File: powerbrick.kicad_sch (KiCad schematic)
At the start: 4 parts, among them U4 TLV62568DBV

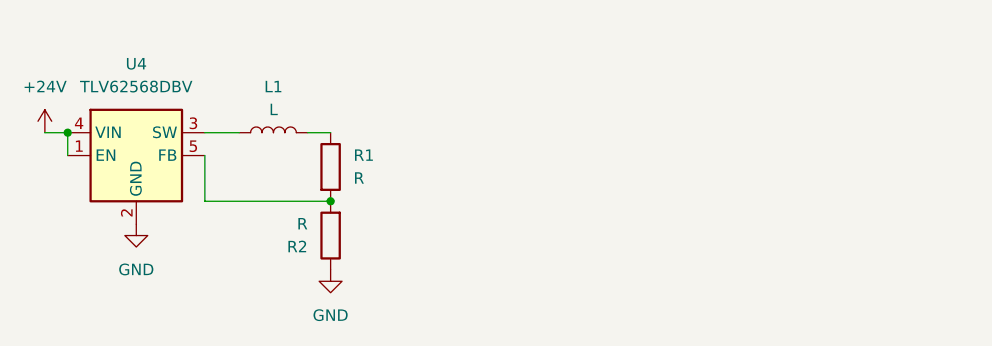
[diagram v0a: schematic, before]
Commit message: power to ICs
updated power brick. added CMOS battery
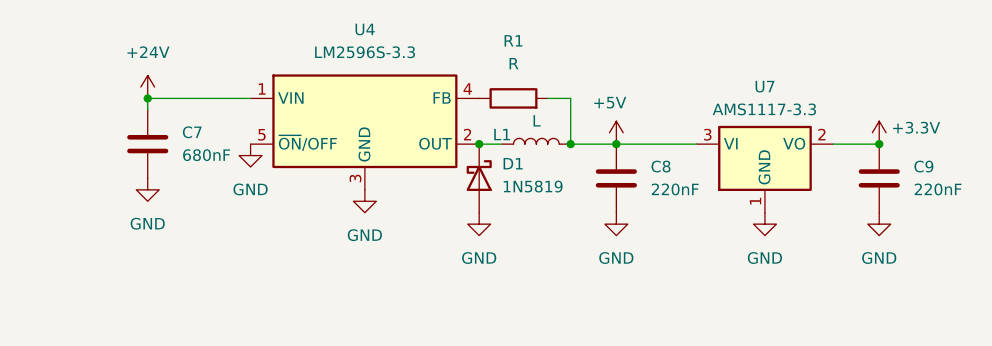
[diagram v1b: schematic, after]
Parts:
- removed R2: R, symbol Device:R
- removed U4: TLV62568DBV, Package_TO_SOT_SMD:SOT-23-5, symbol Regulator_Switching:TLV62568DBV
- added C7: 680nF, symbol Device:C
- added C8, C9: 220nF, symbol Device:C
- added D1: 1N5819, Diode_THT:D_DO-41_SOD81_P10.16mm_Horizontal, symbol Diode:1N5819
- added U4: LM2596S-3.3, Package_TO_SOT_SMD:TO-263-5_TabPin3, symbol Regulator_Switching:LM2596S-3.3
- added U7: AMS1117-3.3, Package_TO_SOT_SMD:SOT-223-3_TabPin2, symbol Regulator_Linear:AMS1117-3.3
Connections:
- net +24V: now also C7.1, U4.1 (VIN)
- net GND: now also C7.2, C8.2, C9.2, D1.2 (A), U4.3 (GND), U4.5 (~{ON}/OFF), U7.1 (GND)
- net at R1.1: now also U4.4 (FB); no longer L1.2
- net +5V: now reaches R1.2
- net +5V: now also L1.2, C8.1, U7.3 (VI)
- net at L1.1: now also D1.1 (K), U4.2 (OUT)
- new net +3.3V: C9.1, U7.2 (VO)
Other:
- moved on the sheet: L1

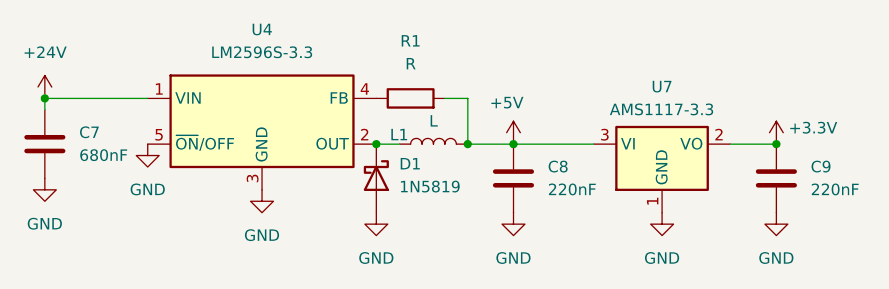
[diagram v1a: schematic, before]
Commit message: Values and finishing touches
I ve seen you put bad values for capacitors in powerbrick and added the value of the feedback resistor, also I redid the inductor circuit because gemini said so and your mosfet was for 20 V not 24 V ...
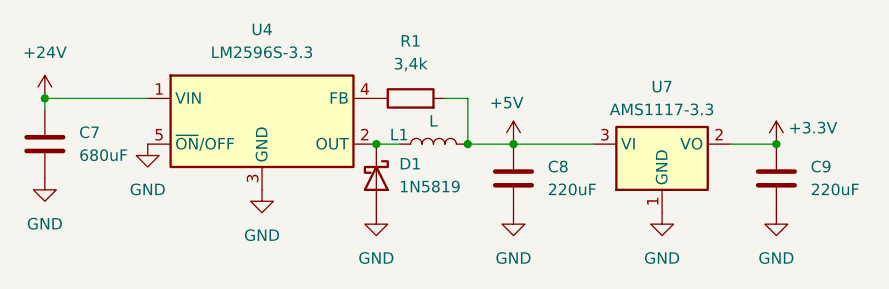
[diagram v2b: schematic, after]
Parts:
- C7: value 680nF -> 680uF
- C8, C9: value 220nF -> 220uF
- R1: value R -> 3,4k
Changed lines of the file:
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@@
 			)
 		)
-		(property "Value" "R"
+		(property "Value" "3,4k"
 			(at 111.76 31.75 90)
 			(effects
@@
 			)
 		)
-		(property "Value" "680nF"
+		(property "Value" "680uF"
 			(at 74.93 41.9099 0)
 			(effects
@@
 			)
 		)
-		(property "Value" "220nF"
+		(property "Value" "220uF"
 			(at 156.21 45.7199 0)
 			(effects
@@
 			)
 		)
-		(property "Value" "220nF"
+		(property "Value" "220uF"
 			(at 127 45.7199 0)
 			(effects

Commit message: .
označení sekcí
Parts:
- added C10: 220nF, symbol Device:C
- C9: value 220uF -> 220nF
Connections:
- net +5V: now also C10.1
- net GND: now also C10.2
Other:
- moved on the sheet: C9, U7
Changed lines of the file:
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@@
 	)
 	(junction
-		(at 152.4 40.64)
+		(at 165.1 40.64)
+		(diameter 0)
+		(color 0 0 0 0)
+	)
+	(junction
+		(at 135.89 40.64)
 		(diameter 0)
 		(color 0 0 0 0)
@@
 	(wire
 		(pts
-			(xy 123.19 40.64) (xy 132.08 40.64)
+			(xy 123.19 40.64) (xy 135.89 40.64)
 		)
 		(stroke
@@
 	(wire
 		(pts
-			(xy 71.12 35.56) (xy 71.12 36.83)
+			(xy 135.89 40.64) (xy 144.78 40.64)
 		)
 		(stroke
@@
 	(wire
 		(pts
-			(xy 118.11 35.56) (xy 118.11 40.64)
+			(xy 71.12 35.56) (xy 71.12 36.83)
 		)
 		(stroke
@@
 	(wire
 		(pts
-			(xy 71.12 35.56) (xy 82.55 35.56)
+			(xy 118.11 35.56) (xy 118.11 40.64)
 		)
 		(stroke
@@
 	(wire
 		(pts
-			(xy 118.11 40.64) (xy 123.19 40.64)
+			(xy 71.12 35.56) (xy 82.55 35.56)
 		)
 		(stroke
@@
 	(wire
 		(pts
-			(xy 152.4 40.64) (xy 147.32 40.64)
+			(xy 118.11 40.64) (xy 123.19 40.64)
 		)
 		(stroke
@@
 		)
 	)
+	(wire
+		(pts
+			(xy 165.1 40.64) (xy 160.02 40.64)
+		)
+		(stroke
+			(width 0)
+			(type default)
+		)
+	)
 	(symbol
 		(lib_id "Device:R")
@@
 	)
 	(symbol
+		(lib_id "Device:C")
+		(at 135.89 44.45 0)
+		(unit 1)
+		(exclude_from_sim no)
+		(in_bom yes)
+		(on_board yes)
+		(dnp no)
+		(fields_autoplaced yes)
+		(property "Reference" "C10"
+			(at 139.7 43.1799 0)
+			(effects
+				(font
+					(size 1.27 1.27)
+				)
+				(justify left)
+			)
+		)
+		(property "Value" "220nF"
+			(at 139.7 45.7199 0)
+			(effects
+				(font
+					(size 1.27 1.27)
+				)
+				(justify left)
+			)
+		)
+		(property "Footprint" ""
+			(at 136.8552 48.26 0)
+			(effects
+				(font
+					(size 1.27 1.27)
+				)
+				(hide yes)
+			)
+		)
+		(property "Datasheet" "~"
+			(at 135.89 44.45 0)
+			(effects
+				(font
+					(size 1.27 1.27)
+				)
+				(hide yes)
+			)
+		)
+		(property "Description" "Unpolarized capacitor"
+			(at 135.89 44.45 0)
+			(effects
+				(font
+					(size 1.27 1.27)
+				)
+				(hide yes)
+			)
+		)
+		(pin "1"
+		)
+		(pin "2"
+		)
+		(instances
+			(project "TechStarter"
+				(path "/7ea2363f-6757-4fc6-83f2-16ce190d79d1/efa4ad20-026b-4f4f-bd8d-a347b34e01c5"
+					(reference "C10")
+					(unit 1)
+				)
+			)
+		)
+	)
+	(symbol
 		(lib_id "power:GND")
 		(at 123.19 48.26 0)
@@
 	(symbol
 		(lib_id "power:+3.3V")
-		(at 152.4 40.64 0)
+		(at 165.1 40.64 0)
 		(unit 1)
 		(exclude_from_sim no)
@@
 		(dnp no)
 		(property "Reference" "#PWR032"
-			(at 152.4 44.45 0)
+			(at 165.1 44.45 0)
 			(effects
 				(font
@@
 		)
 		(property "Value" "+3.3V"
-			(at 156.464 38.862 0)
-			(effects
-				(font
-					(size 1.27 1.27)
-				)
-			)
-		)
-		(property "Footprint" ""
-			(at 152.4 40.64 0)
+			(at 169.164 38.862 0)
+			(effects
+				(font
+					(size 1.27 1.27)
+				)
+			)
+		)
+		(property "Footprint" ""
+			(at 165.1 40.64 0)
 			(effects
 				(font
@@
 		)
 		(property "Datasheet" ""
-			(at 152.4 40.64 0)
+			(at 165.1 40.64 0)
 			(effects
 				(font
@@
 		)
 		(property "Description" "Power symbol creates a global label with name \"+3.3V\""
-			(at 152.4 40.64 0)
+			(at 165.1 40.64 0)
 			(effects
 				(font
@@
 	(symbol
 		(lib_id "power:GND")
-		(at 139.7 48.26 0)
+		(at 152.4 48.26 0)
 		(unit 1)
 		(exclude_from_sim no)
@@
 		(fields_autoplaced yes)
 		(property "Reference" "#PWR027"
-			(at 139.7 54.61 0)
+			(at 152.4 54.61 0)
 			(effects
 				(font
@@
 		)
 		(property "Value" "GND"
-			(at 139.7 53.34 0)
-			(effects
-				(font
-					(size 1.27 1.27)
-				)
-			)
-		)
-		(property "Footprint" ""
-			(at 139.7 48.26 0)
+			(at 152.4 53.34 0)
+			(effects
+				(font
+					(size 1.27 1.27)
+				)
+			)
+		)
+		(property "Footprint" ""
+			(at 152.4 48.26 0)
 			(effects
 				(font
@@
 		)
 		(property "Datasheet" ""
-			(at 139.7 48.26 0)
+			(at 152.4 48.26 0)
 			(effects
 				(font
@@
 		)
 		(property "Description" "Power symbol creates a global label with name \"GND\" , ground"
-			(at 139.7 48.26 0)
+			(at 152.4 48.26 0)
 			(effects
 				(font
@@
 	(symbol
 		(lib_id "power:GND")
-		(at 152.4 48.26 0)
+		(at 165.1 48.26 0)
 		(unit 1)
 		(exclude_from_sim no)
@@
 		(fields_autoplaced yes)
 		(property "Reference" "#PWR030"
-			(at 152.4 54.61 0)
+			(at 165.1 54.61 0)
 			(effects
 				(font
@@
 		)
 		(property "Value" "GND"
-			(at 152.4 53.34 0)
-			(effects
-				(font
-					(size 1.27 1.27)
-				)
-			)
-		)
-		(property "Footprint" ""
-			(at 152.4 48.26 0)
+			(at 165.1 53.34 0)
+			(effects
+				(font
+					(size 1.27 1.27)
+				)
+			)
+		)
+		(property "Footprint" ""
+			(at 165.1 48.26 0)
 			(effects
 				(font
@@
 		)
 		(property "Datasheet" ""
-			(at 152.4 48.26 0)
+			(at 165.1 48.26 0)
 			(effects
 				(font
@@
 		)
 		(property "Description" "Power symbol creates a global label with name \"GND\" , ground"
-			(at 152.4 48.26 0)
+			(at 165.1 48.26 0)
 			(effects
 				(font
@@
 	)
 	(symbol
+		(lib_id "power:GND")
+		(at 135.89 48.26 0)
+		(unit 1)
+		(exclude_from_sim no)
+		(in_bom yes)
+		(on_board yes)
+		(dnp no)
+		(fields_autoplaced yes)
+		(property "Reference" "#PWR057"
+			(at 135.89 54.61 0)
+			(effects
+				(font
+					(size 1.27 1.27)
+				)
+				(hide yes)
+			)
+		)
+		(property "Value" "GND"
+			(at 135.89 53.34 0)
+			(effects
+				(font
+					(size 1.27 1.27)
+				)
+			)
+		)
+		(property "Footprint" ""
+			(at 135.89 48.26 0)
+			(effects
+				(font
+					(size 1.27 1.27)
+				)
+				(hide yes)
+			)
+		)
+		(property "Datasheet" ""
+			(at 135.89 48.26 0)
+			(effects
+				(font
+					(size 1.27 1.27)
+				)
+				(hide yes)
+			)
+		)
+		(property "Description" "Power symbol creates a global label with name \"GND\" , ground"
+			(at 135.89 48.26 0)
+			(effects
+				(font
+					(size 1.27 1.27)
+				)
+				(hide yes)
+			)
+		)
+		(pin "1"
+		)
+		(instances
+			(project "TechStarter"
+				(path "/7ea2363f-6757-4fc6-83f2-16ce190d79d1/efa4ad20-026b-4f4f-bd8d-a347b34e01c5"
+					(reference "#PWR057")
+					(unit 1)
+				)
+			)
+		)
+	)
+	(symbol
 		(lib_id "Device:C")
-		(at 152.4 44.45 0)
+		(at 165.1 44.45 0)
 		(unit 1)
 		(exclude_from_sim no)
@@
 		(fields_autoplaced yes)
 		(property "Reference" "C9"
-			(at 156.21 43.1799 0)
+			(at 168.91 43.1799 0)
 			(effects
 				(font
@@
 			)
 		)
-		(property "Value" "220uF"
-			(at 156.21 45.7199 0)
+		(property "Value" "220nF"
+			(at 168.91 45.7199 0)
 			(effects
 				(font
@@
 		)
 		(property "Footprint" ""
-			(at 153.3652 48.26 0)
+			(at 166.0652 48.26 0)
 			(effects
 				(font
@@
 		)
 		(property "Datasheet" "~"
-			(at 152.4 44.45 0)
+			(at 165.1 44.45 0)
 			(effects
 				(font
@@
 		)
 		(property "Description" "Unpolarized capacitor"
-			(at 152.4 44.45 0)
+			(at 165.1 44.45 0)
 			(effects
 				(font
@@
 	(symbol
 		(lib_id "Regulator_Linear:AMS1117-3.3")
-		(at 139.7 40.64 0)
+		(at 152.4 40.64 0)
 		(unit 1)
 		(exclude_from_sim no)
@@
 		(fields_autoplaced yes)
 		(property "Reference" "U7"
-			(at 139.7 34.29 0)
+			(at 152.4 34.29 0)
 			(effects
 				(font
@@
 		)
 		(property "Value" "AMS1117-3.3"
-			(at 139.7 36.83 0)
+			(at 152.4 36.83 0)
 			(effects
 				(font
@@
 		)
 		(property "Footprint" "Package_TO_SOT_SMD:SOT-223-3_TabPin2"
-			(at 139.7 35.56 0)
+			(at 152.4 35.56 0)
 			(effects
 				(font
@@
 		)
 		(property "Datasheet" "http://www.advanced-monolithic.com/pdf/ds1117.pdf"
-			(at 142.24 46.99 0)
+			(at 154.94 46.99 0)
 			(effects
 				(font
@@
 		)
 		(property "Description" "1A Low Dropout regulator, positive, 3.3V fixed output, SOT-223"
-			(at 139.7 40.64 0)
-			(effects
-				(font
+			(at 152.4 40.64 0)
+			(effects
+				(font

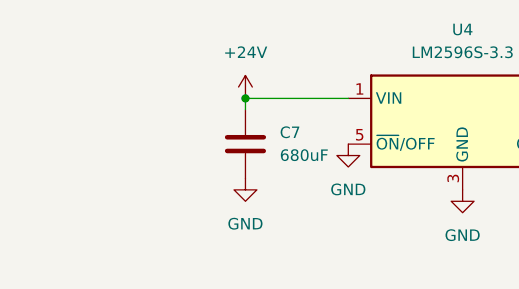
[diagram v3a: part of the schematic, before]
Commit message: Robot I/O
připojil jsem výstup a input z robota přes optočleny a přidal konektor na napájení 24 V
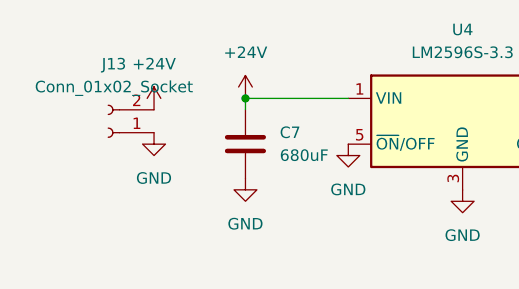
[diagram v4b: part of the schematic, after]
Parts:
- added J13: Conn_01x02_Socket, symbol Connector:Conn_01x02_Socket
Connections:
- net +24V: now also J13.2 (Pin_2)
- net GND: now also J13.1 (Pin_1)
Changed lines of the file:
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@@
+	)
+	(symbol
+		(lib_id "power:+24V")
+		(at 60.96 36.83 0)
+		(unit 1)
+		(exclude_from_sim no)
+		(in_bom yes)
+		(on_board yes)
+		(dnp no)
+		(fields_autoplaced yes)
+		(property "Reference" "#PWR058"
+			(at 60.96 40.64 0)
+			(effects
+				(font
+					(size 1.27 1.27)
+				)
+				(hide yes)
+			)
+		)
+		(property "Value" "+24V"
+			(at 60.96 31.75 0)
+			(effects
+				(font
+					(size 1.27 1.27)
+				)
+			)
+		)
+		(property "Footprint" ""
+			(at 60.96 36.83 0)
+			(effects
+				(font
+					(size 1.27 1.27)
+				)
+				(hide yes)
+			)
+		)
+		(property "Datasheet" ""
+			(at 60.96 36.83 0)
+			(effects
+				(font
+					(size 1.27 1.27)
+				)
+				(hide yes)
+			)
+		)
+		(property "Description" "Power symbol creates a global label with name \"+24V\""
+			(at 60.96 36.83 0)
+			(effects
+				(font
+					(size 1.27 1.27)
+				)
+				(hide yes)
+			)
+		)
+		(pin "1"
+		)
+		(instances
+			(project "TechStarter"
+				(path "/7ea2363f-6757-4fc6-83f2-16ce190d79d1/efa4ad20-026b-4f4f-bd8d-a347b34e01c5"
+					(reference "#PWR058")
+					(unit 1)
+				)
+			)
+		)
 	)
 	(symbol
@@
 					(unit 1)
 				)
+			)
+		)
+	)
+	(symbol
+		(lib_id "power:GND")
+		(at 60.96 39.37 0)
+		(unit 1)
+		(exclude_from_sim no)
+		(in_bom yes)
+		(on_board yes)
+		(dnp no)
+		(fields_autoplaced yes)
+		(property "Reference" "#PWR059"
+			(at 60.96 45.72 0)
+			(effects
+				(font
+					(size 1.27 1.27)
+				)
+				(hide yes)
+			)
+		)
+		(property "Value" "GND"
+			(at 60.96 44.45 0)
+			(effects
+				(font
+					(size 1.27 1.27)
+				)
+			)
+		)
+		(property "Footprint" ""
+			(at 60.96 39.37 0)
+			(effects
+				(font
+					(size 1.27 1.27)
+				)
+				(hide yes)
+			)
+		)
+		(property "Datasheet" ""
+			(at 60.96 39.37 0)
+			(effects
+				(font
+					(size 1.27 1.27)
+				)
+				(hide yes)
+			)
+		)
+		(property "Description" "Power symbol creates a global label with name \"GND\" , ground"
+			(at 60.96 39.37 0)
+			(effects
+				(font
+					(size 1.27 1.27)
+				)
+				(hide yes)
+			)
+		)
+		(pin "1"
+		)
+		(instances
+			(project "TechStarter"
+				(path "/7ea2363f-6757-4fc6-83f2-16ce190d79d1/efa4ad20-026b-4f4f-bd8d-a347b34e01c5"
+					(reference "#PWR059")
+					(unit 1)
+				)
+			)
+		)
+	)
+	(symbol
+		(lib_id "Connector:Conn_01x02_Socket")
+		(at 55.88 39.37 180)
+		(unit 1)
+		(exclude_from_sim no)
+		(in_bom yes)
+		(on_board yes)
+		(dnp no)
+		(fields_autoplaced yes)
+		(property "Reference" "J13"
+			(at 56.515 31.75 0)
+			(effects
+				(font
+					(size 1.27 1.27)
+				)
+			)
+		)
+		(property "Value" "Conn_01x02_Socket"
+			(at 56.515 34.29 0)
+			(effects
+				(font
+					(size 1.27 1.27)
+				)
+			)
+		)
+		(property "Footprint" ""
+			(at 55.88 39.37 0)
+			(effects
+				(font
+					(size 1.27 1.27)
+				)
+				(hide yes)
+			)
+		)
+		(property "Datasheet" "~"
+			(at 55.88 39.37 0)
+			(effects
+				(font
+					(size 1.27 1.27)
+				)
+				(hide yes)
+			)
+		)
+		(property "Description" "Generic connector, single row, 01x02, script generated"
+			(at 55.88 39.37 0)
+			(effects
+				(font
+					(size 1.27 1.27)
+				)
+				(hide yes)
+			)
+		)
+		(pin "2"
+		)
+		(pin "1"
+		)
+		(instances
+			(project ""
+				(path "/7ea2363f-6757-4fc6-83f2-16ce190d79d1/efa4ad20-026b-4f4f-bd8d-a347b34e01c5"
+					(reference "J13")
+					(unit 1)
+				)

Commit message: .
sortation of things, added variant B
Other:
- moved on the sheet: J13
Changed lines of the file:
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@@
 	(symbol
 		(lib_id "power:+24V")
-		(at 60.96 36.83 0)
-		(unit 1)
-		(exclude_from_sim no)
-		(in_bom yes)
-		(on_board yes)
-		(dnp no)
-		(fields_autoplaced yes)
+		(at 41.91 35.56 0)
+		(unit 1)
+		(exclude_from_sim no)
+		(in_bom yes)
+		(on_board yes)
+		(dnp no)
 		(property "Reference" "#PWR058"
-			(at 60.96 40.64 0)
+			(at 41.91 39.37 0)
 			(effects
 				(font
@@
 		)
 		(property "Value" "+24V"
-			(at 60.96 31.75 0)
-			(effects
-				(font
-					(size 1.27 1.27)
-				)
-			)
-		)
-		(property "Footprint" ""
-			(at 60.96 36.83 0)
+			(at 45.212 32.766 0)
+			(effects
+				(font
+					(size 1.27 1.27)
+				)
+			)
+		)
+		(property "Footprint" ""
+			(at 41.91 35.56 0)
 			(effects
 				(font
@@
 		)
 		(property "Datasheet" ""
-			(at 60.96 36.83 0)
+			(at 41.91 35.56 0)
 			(effects
 				(font
@@
 		)
 		(property "Description" "Power symbol creates a global label with name \"+24V\""
-			(at 60.96 36.83 0)
+			(at 41.91 35.56 0)
 			(effects
 				(font
@@
 	(symbol
 		(lib_id "power:GND")
-		(at 60.96 39.37 0)
+		(at 41.91 38.1 0)
 		(unit 1)
 		(exclude_from_sim no)
@@
 		(fields_autoplaced yes)
 		(property "Reference" "#PWR059"
-			(at 60.96 45.72 0)
+			(at 41.91 44.45 0)
 			(effects
 				(font
@@
 		)
 		(property "Value" "GND"
-			(at 60.96 44.45 0)
-			(effects
-				(font
-					(size 1.27 1.27)
-				)
-			)
-		)
-		(property "Footprint" ""
-			(at 60.96 39.37 0)
+			(at 41.91 43.18 0)
+			(effects
+				(font
+					(size 1.27 1.27)
+				)
+			)
+		)
+		(property "Footprint" ""
+			(at 41.91 38.1 0)
 			(effects
 				(font
@@
 		)
 		(property "Datasheet" ""
-			(at 60.96 39.37 0)
+			(at 41.91 38.1 0)
 			(effects
 				(font
@@
 		)
 		(property "Description" "Power symbol creates a global label with name \"GND\" , ground"
-			(at 60.96 39.37 0)
+			(at 41.91 38.1 0)
 			(effects
 				(font
@@
 	(symbol
 		(lib_id "Connector:Conn_01x02_Socket")
-		(at 55.88 39.37 180)
-		(unit 1)
-		(exclude_from_sim no)
-		(in_bom yes)
-		(on_board yes)
-		(dnp no)
-		(fields_autoplaced yes)
+		(at 36.83 38.1 180)
+		(unit 1)
+		(exclude_from_sim no)
+		(in_bom yes)
+		(on_board yes)
+		(dnp no)
 		(property "Reference" "J13"
-			(at 56.515 31.75 0)
+			(at 37.465 30.48 0)
 			(effects
 				(font
@@
 		)
 		(property "Value" "Conn_01x02_Socket"
-			(at 56.515 34.29 0)
-			(effects
-				(font
-					(size 1.27 1.27)
-				)
-			)
-		)
-		(property "Footprint" ""
-			(at 55.88 39.37 0)
+			(at 30.226 33.274 0)
+			(effects
+				(font
+					(size 1.27 1.27)
+				)
+			)
+		)
+		(property "Footprint" ""
+			(at 36.83 38.1 0)
 			(effects
 				(font
@@
 		)
 		(property "Datasheet" "~"
-			(at 55.88 39.37 0)
+			(at 36.83 38.1 0)
 			(effects
 				(font
@@
 		)
 		(property "Description" "Generic connector, single row, 01x02, script generated"
-			(at 55.88 39.37 0)
-			(effects
-				(font
+			(at 36.83 38.1 0)
+			(effects
+				(font

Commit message: Board
started board ...
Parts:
- C10, C9: value 220nF -> 220nF/6,3V; footprint (none) -> Capacitor_SMD:C_0603_1608Metric
- C7: value 680uF -> 680uF/35V; footprint (none) -> Capacitor_SMD:C_Elec_10x10.2
- C8: value 220uF -> 220uF/6,3V; footprint (none) -> Capacitor_SMD:C_Elec_6.3x5.4
- R1: footprint (none) -> Resistor_SMD:R_0603_1608Metric
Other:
- moved on the sheet: C7
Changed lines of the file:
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@@
+	(wire
+		(pts
+			(xy 71.12 43.18) (xy 71.12 44.45)
+		)
+		(stroke
+			(width 0)
+			(type default)
+		)
+	)
 	(wire
 		(pts
@@
 	(wire
 		(pts
-			(xy 71.12 35.56) (xy 71.12 36.83)
+			(xy 118.11 35.56) (xy 118.11 40.64)
 		)
 		(stroke
@@
 	(wire
 		(pts
-			(xy 118.11 35.56) (xy 118.11 40.64)
+			(xy 71.12 35.56) (xy 82.55 35.56)
 		)
 		(stroke
@@
 	(wire
 		(pts
-			(xy 71.12 35.56) (xy 82.55 35.56)
+			(xy 118.11 40.64) (xy 123.19 40.64)
 		)
 		(stroke
@@
 	(wire
 		(pts
-			(xy 118.11 40.64) (xy 123.19 40.64)
+			(xy 165.1 40.64) (xy 160.02 40.64)
 		)
 		(stroke
@@
 		)
 	)
-	(wire
-		(pts
-			(xy 165.1 40.64) (xy 160.02 40.64)
-		)
-		(stroke
-			(width 0)
-			(type default)
-		)
-	)
 	(symbol
 		(lib_id "Device:R")
@@
 			)
 		)
-		(property "Footprint" ""
+		(property "Footprint" "Resistor_SMD:R_0603_1608Metric"
 			(at 111.76 37.338 90)
 			(effects
@@
 		(on_board yes)
 		(dnp no)
-		(fields_autoplaced yes)
 		(property "Reference" "C10"
 			(at 139.7 43.1799 0)
@@
 			)
 		)
-		(property "Value" "220nF"
-			(at 139.7 45.7199 0)
+		(property "Value" "220nF/6,3V"
+			(at 136.906 48.006 0)
 			(effects
 				(font
@@
 			)
 		)
-		(property "Footprint" ""
+		(property "Footprint" "Capacitor_SMD:C_0603_1608Metric"
 			(at 136.8552 48.26 0)
 			(effects
@@
 	(symbol
 		(lib_id "Device:C")
-		(at 71.12 40.64 0)
-		(unit 1)
-		(exclude_from_sim no)
-		(in_bom yes)
-		(on_board yes)
-		(dnp no)
-		(fields_autoplaced yes)
+		(at 71.12 39.37 0)
+		(unit 1)
+		(exclude_from_sim no)
+		(in_bom yes)
+		(on_board yes)
+		(dnp no)
 		(property "Reference" "C7"
-			(at 74.93 39.3699 0)
+			(at 62.23 38.1 0)
 			(effects
 				(font
@@
 			)
 		)
-		(property "Value" "680uF"
-			(at 74.93 41.9099 0)
+		(property "Value" "680uF/35V"
+			(at 57.404 40.64 0)
 			(effects
 				(font
@@
 			)
 		)
-		(property "Footprint" ""
-			(at 72.0852 44.45 0)
+		(property "Footprint" "Capacitor_SMD:C_Elec_10x10.2"
+			(at 72.0852 43.18 0)
 			(effects
 				(font
@@
 		)
 		(property "Datasheet" "~"
-			(at 71.12 40.64 0)
+			(at 71.12 39.37 0)
 			(effects
 				(font
@@
 		)
 		(property "Description" "Unpolarized capacitor"
-			(at 71.12 40.64 0)
+			(at 71.12 39.37 0)
 			(effects
 				(font
@@
 			)
 		)
-		(property "Value" "220nF"
+		(property "Value" "220nF/6,3V"
 			(at 168.91 45.7199 0)
 			(effects
@@
 			)
 		)
-		(property "Footprint" ""
+		(property "Footprint" "Capacitor_SMD:C_0603_1608Metric"
 			(at 166.0652 48.26 0)
 			(effects
@@
 		(on_board yes)
 		(dnp no)
-		(fields_autoplaced yes)
 		(property "Reference" "C8"
 			(at 127 43.1799 0)
@@
 			)
 		)
-		(property "Value" "220uF"
-			(at 127 45.7199 0)
+		(property "Value" "220uF/6,3V"
+			(at 123.952 47.498 0)
 			(effects
 				(font
@@
 			)
 		)
-		(property "Footprint" ""
+		(property "Footprint" "Capacitor_SMD:C_Elec_6.3x5.4"
 			(at 124.1552 48.26 0)
 			(effects
